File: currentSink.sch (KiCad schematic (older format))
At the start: 10 parts

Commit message: updated schematic with MCP4802 and added datasheets
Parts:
- removed U?: MCP4922-E/SL, SO14, symbol MCP4922-E/SL
- added P?: CONN_01X05, symbol CONN_01X05
- added U?: MCP4802-E/SN, SO8, symbol MCP4802-E/SN
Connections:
- wire segments 21 -> 32
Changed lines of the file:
@@
 $EndComp
-$Comp
-L MCP4922-E/SL U?
-U 1 1 5520CE1D
-P 2650 2850
-F 0 "U?" H 2800 3250 40  0000 L BNN
-F 1 "MCP4922-E/SL" H 2800 3200 40  0000 L BNN
-F 2 "SO14" H 2650 2850 30  0000 C CIN
-F 3 "" H 2650 2850 60  0000 C CNN
-	1    2650 2850
-	1    0    0    -1
-$EndComp
-Wire Wire Line
-	5350 3000 3200 3000
-Wire Wire Line
-	5350 2950 5350 3000
-Connection ~ 7700 4650
-Wire Wire Line
-	9350 4650 7700 4650
-Wire Wire Line
-	5750 3500 5750 3600
-Connection ~ 7700 3850
-Wire Wire Line
-	5350 3850 7700 3850
-Wire Wire Line
-	5350 3200 5350 3850
-Wire Wire Line
-	6350 3100 6600 3100
-Wire Wire Line
-	7100 3100 7400 3100
-Wire Wire Line
-	7700 3300 7700 4050
-Wire Wire Line
-	7700 4550 7700 4700
 $Comp
 L TC1016 U?
@@
 	-1   0    0    -1
 $EndComp
-Wire Wire Line
-	2550 1950 6400 1950
-Wire Wire Line
-	5750 1950 5750 2700
-Wire Wire Line
-	2550 2400 2550 1950
-Connection ~ 5750 1950
 $Comp
 L GND #PWR?
@@
 	1    0    0    -1
 $EndComp
-Wire Wire Line
-	6800 2550 6800 2250
-Wire Wire Line
-	7200 1950 9450 1950
-Wire Wire Line
-	7700 2900 7700 1950
-Connection ~ 7700 1950
 $Comp
 L C C?
@@
 	1    0    0    -1
 $EndComp
-Wire Wire Line
-	6200 2150 6200 1950
-Connection ~ 6200 1950
-Wire Wire Line
-	6200 2550 6800 2550
-Connection ~ 7400 1950
-Wire Wire Line
-	7400 2100 7400 1950
-Wire Wire Line
-	7400 2500 6800 2500
-Connection ~ 6800 2500
 $Comp
 L GND #PWR?
@@
 	1    0    0    -1
 $EndComp
+$Comp
+L MCP4802-E/SN U?
+U 1 1 5520E852
+P 2650 2850
+F 0 "U?" H 2650 3200 40  0000 L BNN
+F 1 "MCP4802-E/SN" H 2650 3150 40  0000 L BNN
+F 2 "SO8" H 2650 2850 30  0000 C CIN
+F 3 "" H 2650 2850 60  0000 C CNN
+	1    2650 2850
+	1    0    0    -1
+$EndComp
 Wire Wire Line
-	2550 3300 2550 3550
+	2550 3250 2550 3550
+Wire Wire Line
+	3050 3000 5350 3000
+Wire Wire Line
+	2550 2450 2550 1950
+Connection ~ 6800 2500
+Wire Wire Line
+	7400 2500 6800 2500
+Wire Wire Line
+	7400 2100 7400 1950
+Connection ~ 7400 1950
+Wire Wire Line
+	6800 2550 6200 2550
+Connection ~ 6200 1950
+Wire Wire Line
+	6200 2150 6200 1950
+Connection ~ 7700 1950
+Wire Wire Line
+	7700 2900 7700 1950
+Wire Wire Line
+	7200 1950 9450 1950
+Wire Wire Line
+	6800 2250 6800 2550
+Connection ~ 5750 1950
+Wire Wire Line
+	5750 1950 5750 2700
+Wire Wire Line
+	2550 1950 6400 1950
+Wire Wire Line
+	7700 4550 7700 4700
+Wire Wire Line
+	7700 3300 7700 4050
+Wire Wire Line
+	7100 3100 7400 3100
+Wire Wire Line
+	6350 3100 6600 3100
+Wire Wire Line
+	5350 3200 5350 3850
+Wire Wire Line
+	5350 3850 7700 3850
+Connection ~ 7700 3850
+Wire Wire Line
+	5750 3500 5750 3600
+Wire Wire Line
+	9350 4650 7700 4650
+Connection ~ 7700 4650
+Connection ~ 2550 3400
+$Comp
+L CONN_01X05 P?
+U 1 1 5520F4FB
+P 1300 4300
+F 0 "P?" H 1300 4600 50  0000 C CNN
+F 1 "CONN_01X05" V 1400 4300 50  0000 C CNN
+F 2 "" H 1300 4300 60  0000 C CNN
+F 3 "" H 1300 4300 60  0000 C CNN
+	1    1300 4300
+	-1   0    0    1
+$EndComp
+Wire Wire Line
+	2100 3000 2050 3000
+Wire Wire Line
+	2050 3000 2050 3400
+Wire Wire Line
+	2050 3400 2550 3400
+Wire Wire Line
+	2100 2900 2000 2900
+Wire Wire Line
+	2000 2900 2000 4500
+Wire Wire Line
+	2000 4500 1500 4500
+Wire Wire Line
+	2100 2800 1900 2800
+Wire Wire Line
+	1900 2800 1900 4400
+Wire Wire Line
+	1900 4400 1500 4400
+Wire Wire Line
+	2100 2700 1800 2700
+Wire Wire Line
+	1800 2700 1800 4300
+Wire Wire Line
+	1800 4300 1500 4300
 $EndSCHEMATC

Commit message: added LM2931D-R regulator
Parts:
- removed U?: TC1016, symbol TC1016
- added C? (x2): C, symbol C
- added R?: 27K, symbol R
- added R?: 21.6K, symbol R
- added R?: 0, symbol R
- added U?: LM2931D-R, symbol LM2931D-R
- Q?: value MOSFET_N -> BUK9575; MPN (none) -> BUK9575-100A,127
- R?: value R -> .1; MPN (none) -> AC01000001007JA100
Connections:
- wire segments 32 -> 49
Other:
- moved on the sheet: C?, P?, U?A

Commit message: added new sheets currentControl, powerRegulatio, uControl and voltageControl
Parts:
- removed C? (x4): C, symbol C
- removed P?: CONN_01X05, symbol CONN_01X05
- removed Q?: BUK9575, symbol MOSFET_N
- removed R?: .1, symbol R
- removed R?: R, symbol R
- removed R?: 27K, symbol R
- removed R?: 21.6K, symbol R
- removed R?: 0, symbol R
- removed U?: LMV358, symbol LMV358
- removed U?: MCP4802-E/SN, SO8, symbol MCP4802-E/SN
- removed U?: LM2931D-R, symbol LM2931D-R
- added P?: CONN_01X05, symbol CONN_01X05
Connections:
- wire segments 49 -> 30
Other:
- moved on the sheet: P?

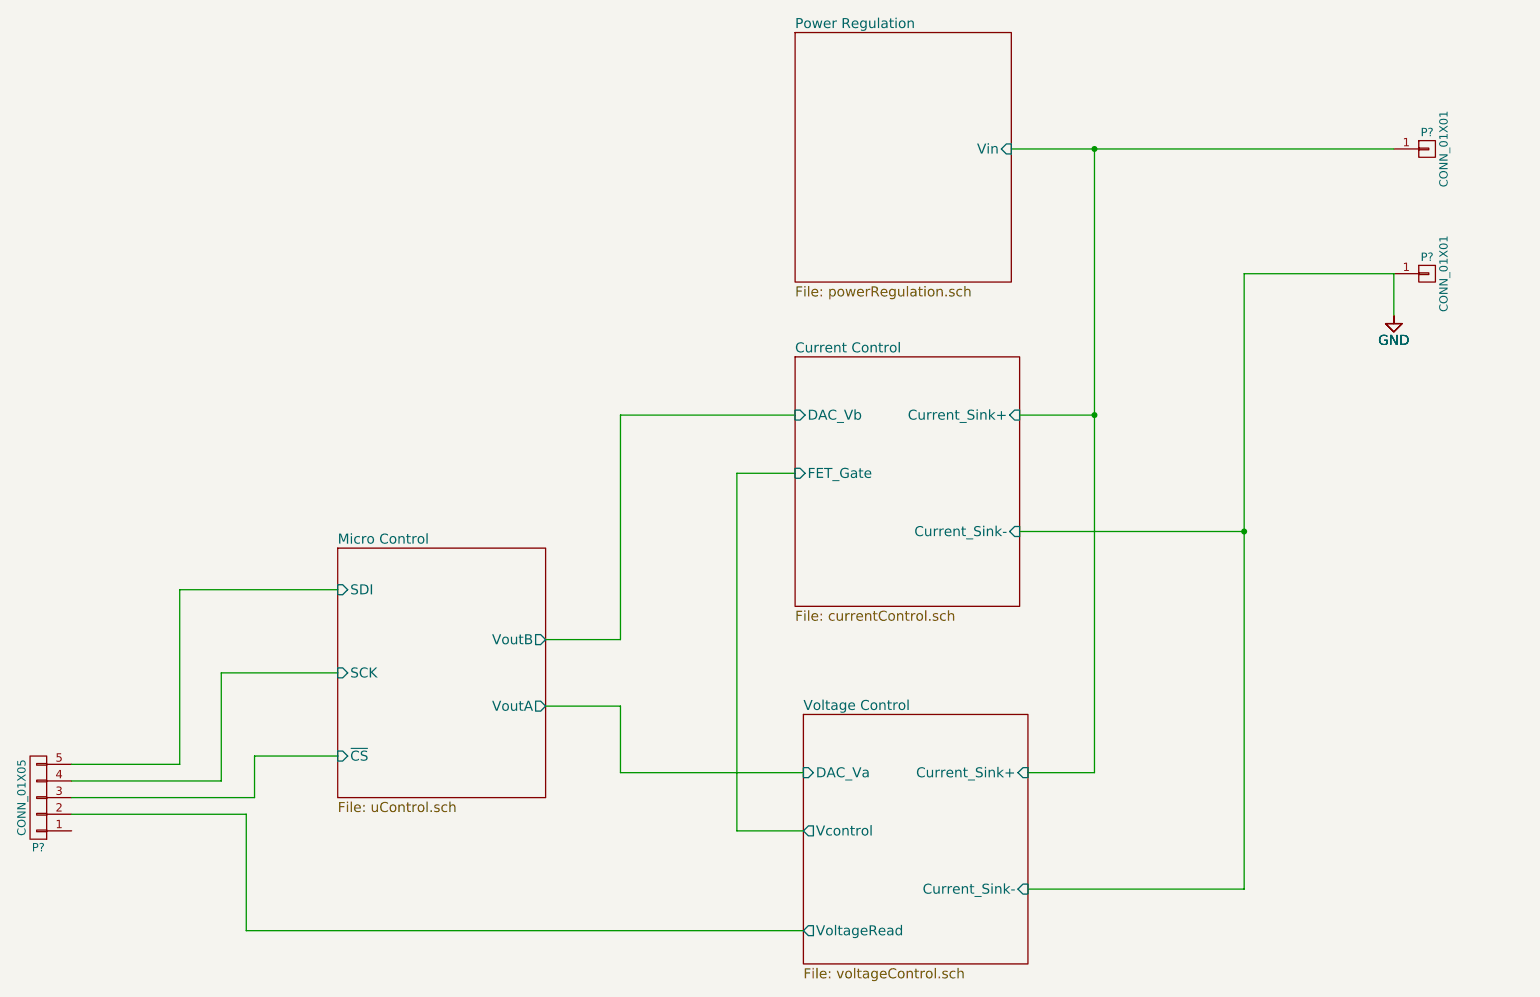
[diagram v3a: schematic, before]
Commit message: updated schematic with current read
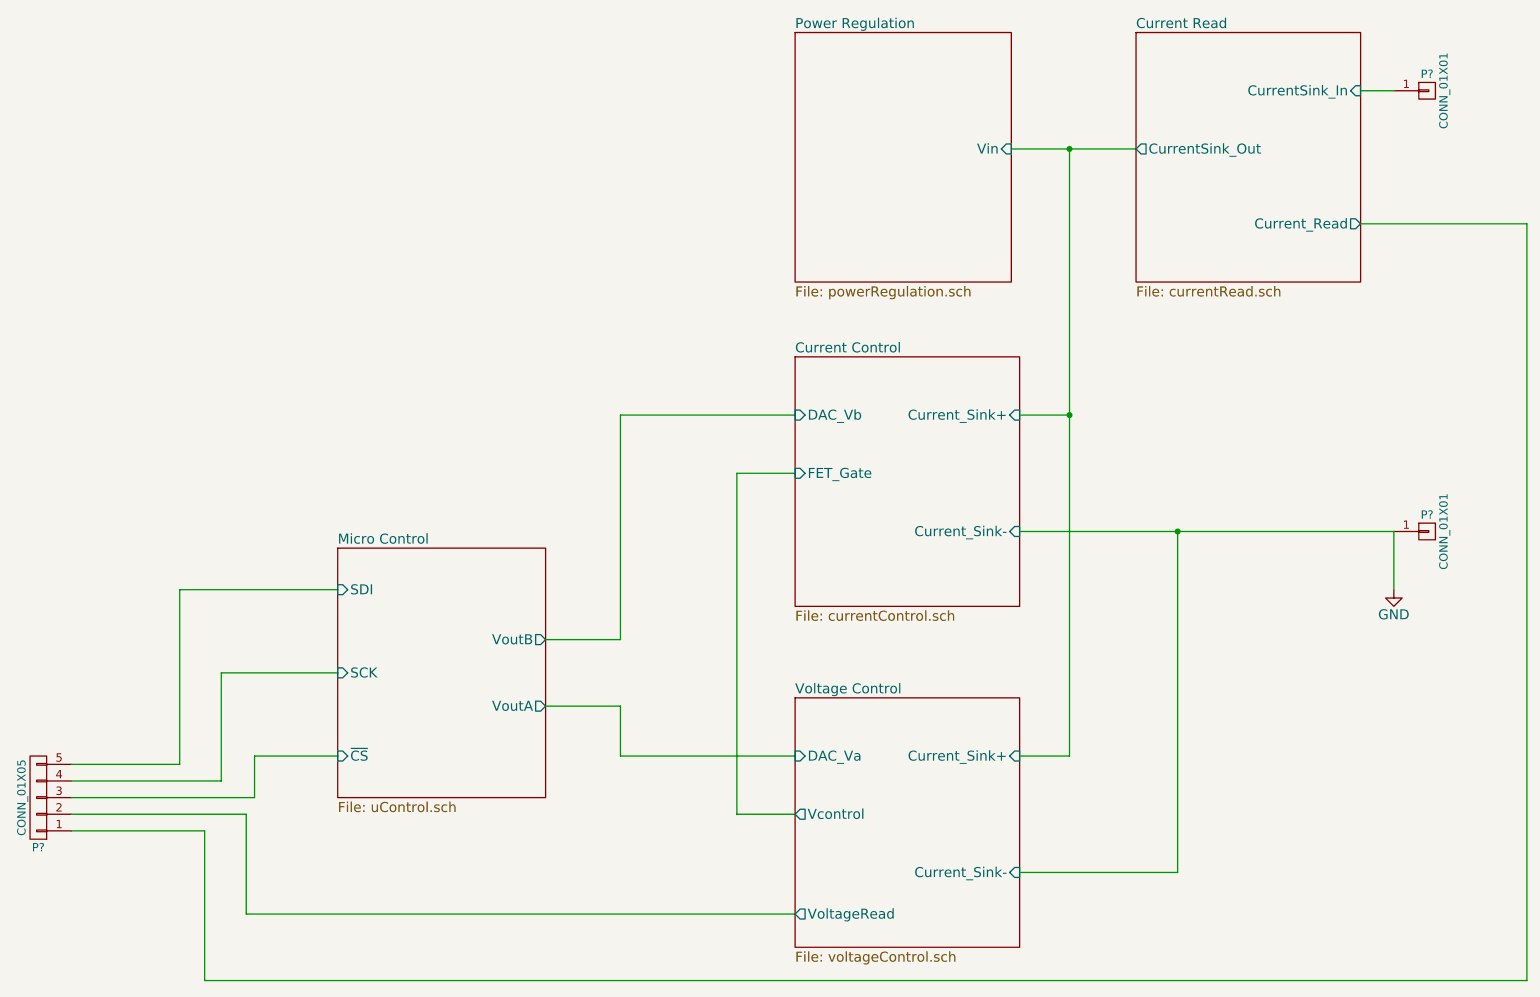
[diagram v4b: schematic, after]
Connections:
- net Current Control/Current_Sink+: no longer P?.1 (P1)
- net Current Read/Current_Read: now reaches P?.1 (P1)
- new net Current Read/CurrentSink_In: P?.1 (P1)
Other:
- moved on the sheet: P?
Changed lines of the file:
@@
 $Descr A4 11693 8268
 encoding utf-8
-Sheet 1 5
+Sheet 1 6
 Title ""
 Date ""
@@
 L CONN_01X01 P?
 U 1 1 5520CA7E
-P 9650 2150
-F 0 "P?" H 9650 2250 50  0000 C CNN
-F 1 "CONN_01X01" V 9750 2150 50  0000 C CNN
-F 2 "" H 9650 2150 60  0000 C CNN
-F 3 "" H 9650 2150 60  0000 C CNN
-	1    9650 2150
+P 9650 3700
+F 0 "P?" H 9650 3800 50  0000 C CNN
+F 1 "CONN_01X01" V 9750 3700 50  0000 C CNN
+F 2 "" H 9650 3700 60  0000 C CNN
+F 3 "" H 9650 3700 60  0000 C CNN
+	1    9650 3700
 	1    0    0    -1
 $EndComp
@@
 L CONN_01X01 P?
 U 1 1 5520CAE0
-P 9650 1400
-F 0 "P?" H 9650 1500 50  0000 C CNN
-F 1 "CONN_01X01" V 9750 1400 50  0000 C CNN
-F 2 "" H 9650 1400 60  0000 C CNN
-F 3 "" H 9650 1400 60  0000 C CNN
-	1    9650 1400
+P 9650 1050
+F 0 "P?" H 9650 1150 50  0000 C CNN
+F 1 "CONN_01X01" V 9750 1050 50  0000 C CNN
+F 2 "" H 9650 1050 60  0000 C CNN
+F 3 "" H 9650 1050 60  0000 C CNN
+	1    9650 1050
 	1    0    0    -1
 $EndComp
@@
 $EndSheet
 $Sheet
-S 5900 4800 1350 1500
+S 5850 4700 1350 1500
 U 5521306C
 F0 "Voltage Control" 60
 F1 "voltageControl.sch" 60
-F2 "Vcontrol" O L 5900 5500 60
-F3 "Current_Sink+" I R 7250 5150 60
-F4 "Current_Sink-" I R 7250 5850 60
-F5 "DAC_Va" I L 5900 5150 60
-F6 "VoltageRead" O L 5900 6100 60
+F2 "Vcontrol" O L 5850 5400 60
+F3 "Current_Sink+" I R 7200 5050 60
+F4 "Current_Sink-" I R 7200 5750 60
+F5 "DAC_Va" I L 5850 5050 60
+F6 "VoltageRead" O L 5850 6000 60
 $EndSheet
 $Comp
@@
 $Comp
 L GND #PWR?
-U 1 1 552165D7
-P 9450 2400
-F 0 "#PWR?" H 9450 2150 60  0001 C CNN
-F 1 "GND" H 9450 2250 60  0000 C CNN
-F 2 "" H 9450 2400 60  0000 C CNN
-F 3 "" H 9450 2400 60  0000 C CNN
-	1    9450 2400
-	1    0    0    -1
-$EndComp
-$Comp
-L GND #PWR?
 U 1 1 552165DD
-P 9450 2400
-F 0 "#PWR?" H 9450 2150 60  0001 C CNN
-F 1 "GND" H 9450 2250 60  0000 C CNN
-F 2 "" H 9450 2400 60  0000 C CNN
-F 3 "" H 9450 2400 60  0000 C CNN
-	1    9450 2400
+P 9450 4050
+F 0 "#PWR?" H 9450 3800 60  0001 C CNN
+F 1 "GND" H 9450 3900 60  0000 C CNN
+F 2 "" H 9450 4050 60  0000 C CNN
+F 3 "" H 9450 4050 60  0000 C CNN
+	1    9450 4050
 	1    0    0    -1
 $EndComp
@@
 $EndSheet
 Wire Wire Line
-	9450 2400 9450 2150
+	5850 5400 5500 5400
 Wire Wire Line
-	7150 1400 9450 1400
-Wire Wire Line
-	5900 5500 5500 5500
-Wire Wire Line
-	5500 5500 5500 3350
+	5500 5400 5500 3350
 Wire Wire Line
 	5500 3350 5850 3350
 Wire Wire Line
-	7200 3000 7650 3000
+	7200 3700 8150 3700
 Wire Wire Line
-	7650 1400 7650 5150
-Connection ~ 7650 1400
+	8150 3700 9450 3700
 Wire Wire Line
-	9450 2150 8550 2150
+	7500 5050 7200 5050
 Wire Wire Line
-	8550 2150 8550 5850
-Wire Wire Line
-	8550 3700 7200 3700
-Wire Wire Line
-	7650 5150 7250 5150
-Connection ~ 7650 3000
-Wire Wire Line
-	8550 5850 7250 5850
-Connection ~ 8550 3700
+	8150 5750 7200 5750
+Connection ~ 8150 3700
 Wire Wire Line
 	4350 4350 4800 4350
@@
 	4350 4750 4800 4750
 Wire Wire Line
-	4800 4750 4800 5150
+	4800 4750 4800 5050
 Wire Wire Line
-	4800 5150 5900 5150
+	4800 5050 5850 5050
 Wire Wire Line
 	3100 5050 2600 5050
@@
 	2150 5100 1500 5100
 Wire Wire Line
-	5900 6100 2550 6100
+	5850 6000 2550 6000
 Wire Wire Line
-	2550 6100 2550 5400
+	2550 6000 2550 5400
 Wire Wire Line
 	2550 5400 1500 5400
+Wire Wire Line
+	9450 3700 9450 4050
+$Sheet
+S 7900 700  1350 1500
+U 5522512A
+F0 "Current Read" 60
+F1 "currentRead.sch" 60
+F2 "CurrentSink_In" I R 9250 1050 60
+F3 "CurrentSink_Out" O L 7900 1400 60
+F4 "Current_Read" O R 9250 1850 60
+$EndSheet
+Wire Wire Line
+	9450 1050 9250 1050
+Wire Wire Line
+	7150 1400 7500 1400
+Wire Wire Line
+	7500 1400 7900 1400
+Wire Wire Line
+	9250 1850 10250 1850
+Wire Wire Line
+	10250 1850 10250 6400
+Wire Wire Line
+	10250 6400 2300 6400
+Wire Wire Line
+	2300 6400 2300 5500
+Wire Wire Line
+	2300 5500 1500 5500
+Wire Wire Line
+	7500 1400 7500 3000
+Wire Wire Line
+	7500 3000 7500 5050
+Connection ~ 7500 1400
+Wire Wire Line
+	7200 3000 7500 3000
+Connection ~ 7500 3000
+Wire Wire Line
+	8150 3700 8150 5750
 $EndSCHEMATC

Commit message: added additional regulator to power the ACS711 and potentially a micro at 3.3V
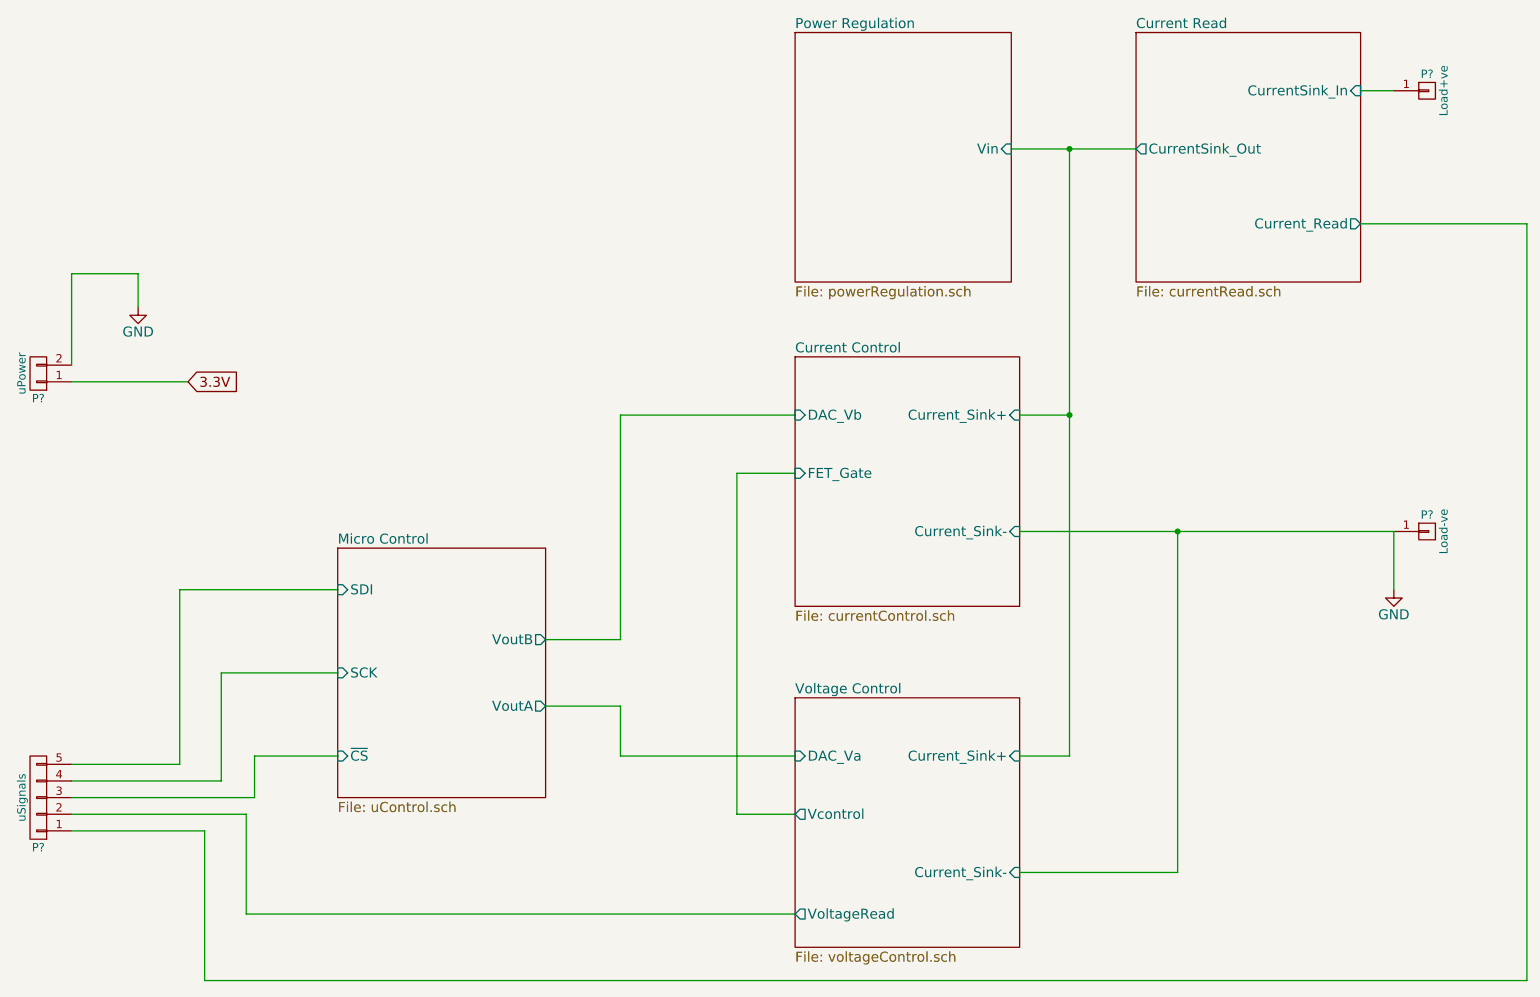
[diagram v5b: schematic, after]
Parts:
- added P?: uPower, symbol CONN_01X02
- P?: value CONN_01X01 -> Load-ve
- P?: value CONN_01X01 -> Load+ve
- P?: value CONN_01X05 -> uSignals
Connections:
- net GND: now also P?.2 (P2)
- new net 3.3V: P?.1 (P1)
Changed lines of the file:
@@
 P 9650 3700
 F 0 "P?" H 9650 3800 50  0000 C CNN
-F 1 "CONN_01X01" V 9750 3700 50  0000 C CNN
+F 1 "Load-ve" V 9750 3700 50  0000 C CNN
 F 2 "" H 9650 3700 60  0000 C CNN
 F 3 "" H 9650 3700 60  0000 C CNN
@@
 P 9650 1050
 F 0 "P?" H 9650 1150 50  0000 C CNN
-F 1 "CONN_01X01" V 9750 1050 50  0000 C CNN
+F 1 "Load+ve" V 9750 1050 50  0000 C CNN
 F 2 "" H 9650 1050 60  0000 C CNN
 F 3 "" H 9650 1050 60  0000 C CNN
@@
 P 1300 5300
 F 0 "P?" H 1300 5600 50  0000 C CNN
-F 1 "CONN_01X05" V 1400 5300 50  0000 C CNN
+F 1 "uSignals" V 1400 5300 50  0000 C CNN
 F 2 "" H 1300 5300 60  0000 C CNN
 F 3 "" H 1300 5300 60  0000 C CNN
@@
 	5500 3350 5850 3350
 Wire Wire Line
-	7200 3700 8150 3700
-Wire Wire Line
-	8150 3700 9450 3700
+	7200 3700 9450 3700
 Wire Wire Line
 	7500 5050 7200 5050
@@
 	9450 1050 9250 1050
 Wire Wire Line
-	7150 1400 7500 1400
-Wire Wire Line
-	7500 1400 7900 1400
+	7150 1400 7900 1400
 Wire Wire Line
 	9250 1850 10250 1850
@@
 	2300 5500 1500 5500
 Wire Wire Line
-	7500 1400 7500 3000
-Wire Wire Line
-	7500 3000 7500 5050
+	7500 1400 7500 5050
 Connection ~ 7500 1400
 Wire Wire Line
@@
 Wire Wire Line
 	8150 3700 8150 5750
+$Comp
+L CONN_01X02 P?
+U 1 1 55229A93
+P 1300 2750
+F 0 "P?" H 1300 2900 50  0000 C CNN
+F 1 "uPower" V 1400 2750 50  0000 C CNN
+F 2 "" H 1300 2750 60  0000 C CNN
+F 3 "" H 1300 2750 60  0000 C CNN
+F 4 "Value" H 1300 2750 60  0001 C CNN "MPN"
+	1    1300 2750
+	-1   0    0    1
+$EndComp
+$Comp
+L GND #PWR?
+U 1 1 55229C45
+P 1900 2350
+F 0 "#PWR?" H 1900 2100 60  0001 C CNN
+F 1 "GND" H 1900 2200 60  0000 C CNN
+F 2 "" H 1900 2350 60  0000 C CNN
+F 3 "" H 1900 2350 60  0000 C CNN
+	1    1900 2350
+	1    0    0    -1
+$EndComp
+Wire Wire Line
+	1500 2700 1500 2150
+Wire Wire Line
+	1500 2150 1900 2150
+Wire Wire Line
+	1900 2150 1900 2350
+Text GLabel 2200 2800 2    60   Input ~ 0
+3.3V
+Wire Wire Line
+	1500 2800 2200 2800
 $EndSCHEMATC
